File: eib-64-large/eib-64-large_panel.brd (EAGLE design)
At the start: 180 x 180 mm, 228 parts, among them J1 DF40-REC, J2 DF40-REC, J3 DF40-REC, J4 DF40-REC, J5 DF40-REC, J6 DF40-REC, J7 DF40-REC, J8 DF40-REC, J9 DF40-REC

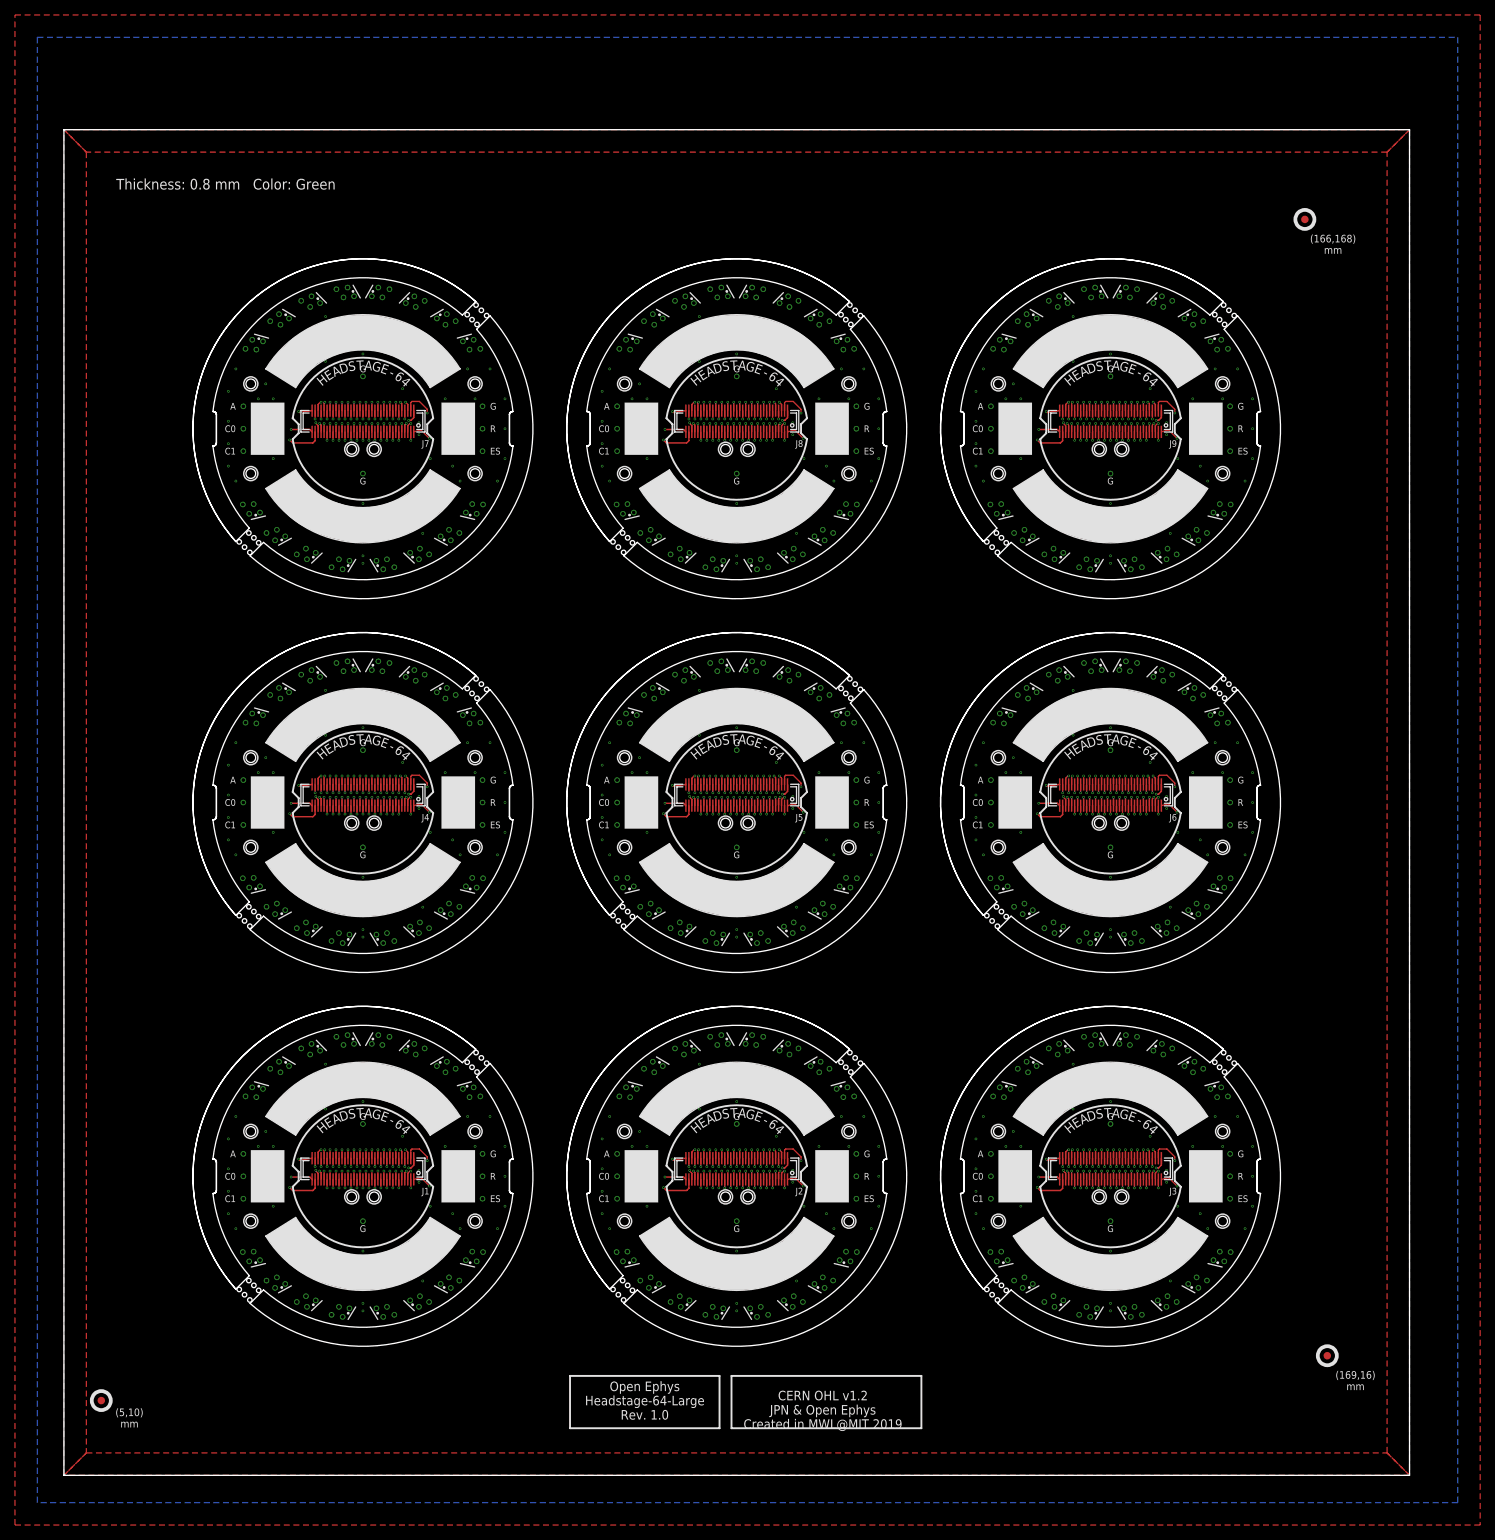
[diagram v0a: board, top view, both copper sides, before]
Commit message: headstage-64 rev. 1.4 along with all dependencies
- This is headstage-64 revision 1.4. Because it involves a change in the
bottom analog connector, a lot of other boards had to be changed to
match the new pinout. That is why there are so many files in this
commit. Changes in revision 1.4 and affects on other boards are as
follows:

1. The coaxial adapter board has been improved to allow a regulator to
sit on the daughter board. To do this, the filtered vcoax had to brought
back to the daughter board and then out again after regulation. Of
course this regulation can be bypassed simply by connecting these
contacts

2. Vcoax decoupling has been greatly improved to lower impedance of
power input. There is now 70 uF of decoupling capacitance on the
post-regulated vcoax.

3. The JTAG interface was changed to allow it to be enabled and disabled
by the programmer. This means that these pins are nominally used for
extra IO. The programmer now contains a jumper that allows it operate in
this new mode (closed) or legacy mode (open) for headstage-64 rev 1.3.

4. All of the serializers GPIO lines are now all routed to the FPGA.

5. The opto and estim circuits no longer share SPI lines so they can be
operated independently.

6. The analog routing to the intan chip has been changed such that the
electrode lines are shielded from vcoax, which was polluting the anlog
signals, by a ground pin. This means that eibs etc. need to respect this
new pinout. This is why eib-64, eib-64-large, nanoz-adapter,
omnetics-adapter-64, and test-board-64 have been changed.

7. The serializer on headstage-64 has been upgraded to DS90UB933-Q1
which has reduced back channel latencies, increased forward channel
bandwidth, and improved performance with
imperfect cabling.

8. There is a solder jumper on the bottom of headstage-64 to allow the
addition of an external resistor to AUXIN3 on the intan to allow it to
operate at lower bandwidths. This comes at the cost of not being able to
measure istim unless t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
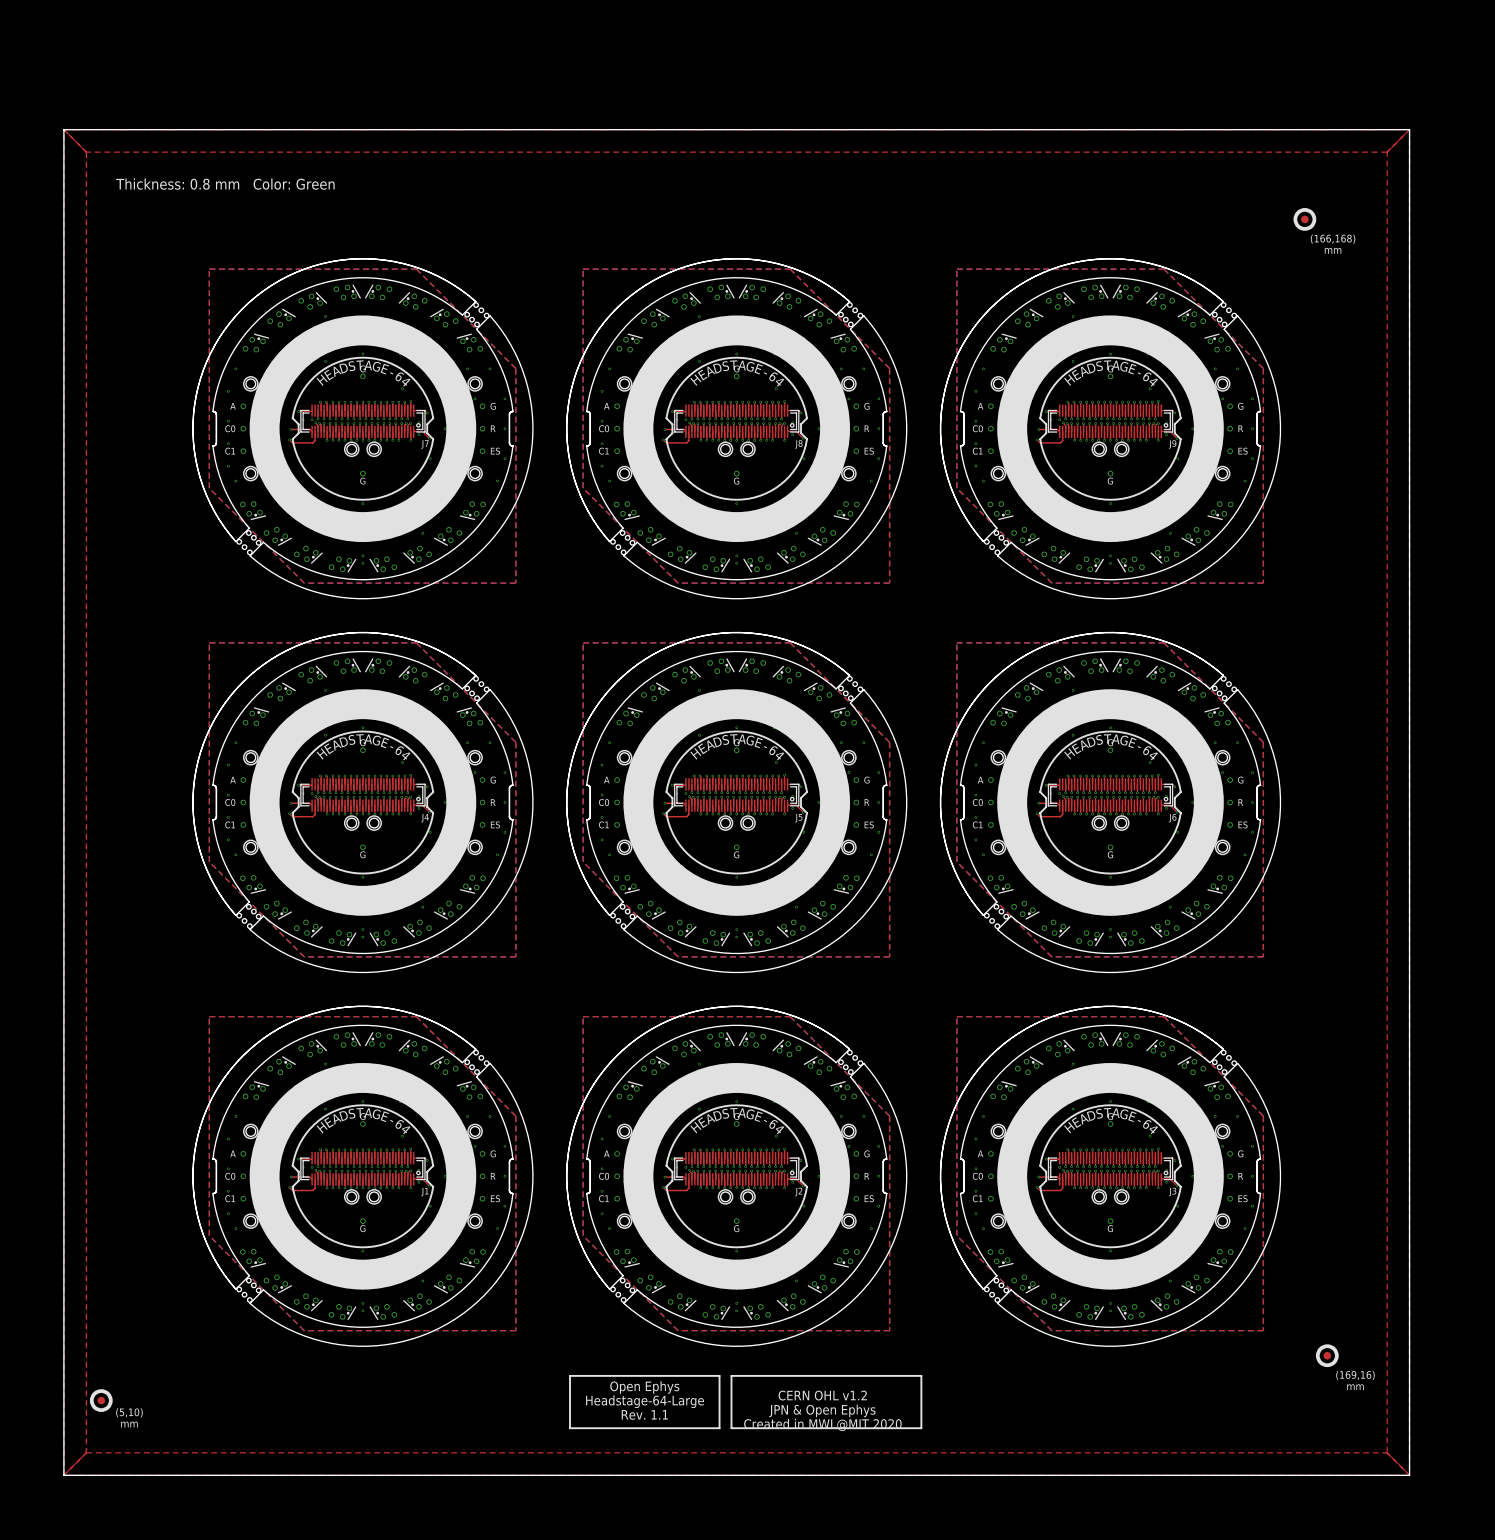
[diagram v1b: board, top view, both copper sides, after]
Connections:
- removed net GND: GND0.P$1, GND1.P$1, GND10.P$1, GND11.P$1, GND12.P$1, GND13.P$1, GND14.P$1, GND15.P$1, GND16.P$1, GND17.P$1, GND2.P$1, GND3.P$1, GND4.P$1, GND5.P$1, GND6.P$1, GND7.P$1, GND8.P$1, GND9.P$1, J1.70, J2.70, J3.70, J4.70, J5.70, J6.70, J7.70, J8.70, J9.70, SHLD_A.P$1, SHLD_A1.P$1, SHLD_A2.P$1, SHLD_A3.P$1, SHLD_A4.P$1, SHLD_A5.P$1, SHLD_A6.P$1, SHLD_A7.P$1, SHLD_A8.P$1
- new net GND1: GND0.P$1, GND1.P$1, J1.37, SHLD_A.P$1
- new net GND2: GND2.P$1, GND3.P$1, J2.37, SHLD_A1.P$1
- new net GND3: GND4.P$1, GND5.P$1, J3.37, SHLD_A2.P$1
- new net GND4: GND6.P$1, GND7.P$1, J4.37, SHLD_A3.P$1
- new net GND5: GND8.P$1, GND9.P$1, J5.37, SHLD_A4.P$1
- new net GND6: GND10.P$1, GND11.P$1, J6.37, SHLD_A5.P$1
- new net GND7: GND12.P$1, GND13.P$1, J7.37, SHLD_A6.P$1
- new net GND8: GND14.P$1, GND15.P$1, J8.37, SHLD_A7.P$1
- new net GND9: GND16.P$1, GND17.P$1, J9.37, SHLD_A8.P$1
- net N$1: now also J1.69; no longer J1.68
- net N$10: now also J1.60; no longer J1.59
- net N$100: now also J2.38; no longer J2.37
- net N$11: now also J1.59; no longer J1.58
- net N$12: now also J1.58; no longer J1.57
- net N$129: now also J3.69; no longer J3.68
- net N$13: now also J1.57; no longer J1.56
- net N$130: now also J3.67; no longer J3.66
- net N$131: now also J3.65; no longer J3.64
- net N$132: now also J3.64; no longer J3.63
- net N$133: now also J3.63; no longer J3.62
- net N$134: now also J3.62; no longer J3.61
- net N$135: now also J3.61; no longer J3.60
- net N$136: now also J3.60; no longer J3.59
- net N$137: now also J3.59; no longer J3.58
- net N$138: now also J3.58; no longer J3.57
- net N$139: now also J3.57; no longer J3.56
- net N$14: now also J1.56; no longer J1.55
- net N$140: now also J3.56; no longer J3.55
- net N$141: now also J3.55; no longer J3.54
- net N$142: now also J3.54; no longer J3.53
- net N$143: now also J3.53; no longer J3.52
- net N$144: now also J3.52; no longer J3.51
- net N$145: now also J3.51; no longer J3.50
- net N$146: now also J3.50; no longer J3.49
- net N$147: now also J3.49; no longer J3.48
- net N$148: now also J3.48; no longer J3.47
- net N$149: now also J3.47; no longer J3.46
- net N$15: now also J1.55; no longer J1.54
- net N$150: now also J3.46; no longer J3.45
- net N$151: now also J3.45; no longer J3.44
- net N$152: now also J3.44; no longer J3.43
- net N$153: now also J3.43; no longer J3.42
- net N$154: now also J3.42; no longer J3.41
- net N$155: now also J3.41; no longer J3.40
- net N$156: now also J3.39; no longer J3.38
- net N$16: now also J1.54; no longer J1.53
- net N$161: now also J3.66; no longer J3.65
- net N$162: now also J3.68; no longer J3.67
- net N$163: now also J3.40; no longer J3.39
- net N$164: now also J3.38; no longer J3.37
- net N$17: now also J1.53; no longer J1.52
- net N$18: now also J1.52; no longer J1.51
- net N$19: now also J1.51; no longer J1.50
- net N$193: now also J4.69; no longer J4.68
- net N$194: now also J4.67; no longer J4.66
- net N$195: now also J4.65; no longer J4.64
- net N$196: now also J4.64; no longer J4.63
- net N$197: now also J4.63; no longer J4.62
- net N$198: now also J4.62; no longer J4.61
- net N$2: now also J1.66; no longer J1.65
- net N$20: now also J1.50; no longer J1.49
- net N$21: now also J1.49; no longer J1.48
- net N$22: now also J1.48; no longer J1.47
- net N$227: now also J4.61; no longer J4.60
- net N$228: now also J4.60; no longer J4.59
- net N$229: now also J4.59; no longer J4.58
- net N$23: now also J1.47; no longer J1.46
- net N$230: now also J4.58; no longer J4.57
- net N$231: now also J4.57; no longer J4.56
- net N$232: now also J4.56; no longer J4.55
- net N$233: now also J4.55; no longer J4.54
- net N$234: now also J4.54; no longer J4.53
- net N$235: now also J4.53; no longer J4.52
- net N$236: now also J4.52; no longer J4.51
- net N$237: now also J4.51; no longer J4.50
- net N$238: now also J4.50; no longer J4.49
- net N$239: now also J4.49; no longer J4.48
- net N$24: now also J1.46; no longer J1.45
- net N$240: now also J4.48; no longer J4.47
- net N$241: now also J4.47; no longer J4.46
- net N$242: now also J4.46; no longer J4.45
- net N$243: now also J4.45; no longer J4.44
- net N$244: now also J4.44; no longer J4.43
- net N$245: now also J4.43; no longer J4.42
- net N$246: now also J4.42; no longer J4.41
- net N$247: now also J4.41; no longer J4.40
- net N$248: now also J4.39; no longer J4.38
- net N$25: now also J1.45; no longer J1.44
- net N$253: now also J4.66; no longer J4.65
- net N$254: now also J4.68; no longer J4.67
- net N$255: now also J4.40; no longer J4.39
- net N$256: now also J4.38; no longer J4.37
- net N$26: now also J1.44; no longer J1.43
- net N$27: now also J1.43; no longer J1.42
- net N$28: now also J1.42; no longer J1.41
- net N$285: now also J5.69; no longer J5.68
- net N$286: now also J5.67; no longer J5.66
- net N$287: now also J5.65; no longer J5.64
- net N$288: now also J5.64; no longer J5.63
- net N$289: now also J5.63; no longer J5.62
- net N$29: now also J1.41; no longer J1.40
- net N$290: now also J5.62; no longer J5.61
- net N$291: now also J5.61; no longer J5.60
- net N$292: now also J5.60; no longer J5.59
- net N$293: now also J5.59; no longer J5.58
- net N$294: now also J5.58; no longer J5.57
- net N$295: now also J5.57; no longer J5.56
- net N$296: now also J5.56; no longer J5.55
- net N$297: now also J5.55; no longer J5.54
- net N$298: now also J5.54; no longer J5.53
- net N$299: now also J5.53; no longer J5.52
- net N$3: now also J1.67; no longer J1.66
- net N$30: now also J1.40; no longer J1.39
- net N$300: now also J5.52; no longer J5.51
- net N$301: now also J5.51; no longer J5.50
- net N$302: now also J5.50; no longer J5.49
- net N$303: now also J5.49; no longer J5.48
- net N$304: now also J5.48; no longer J5.47
- net N$305: now also J5.47; no longer J5.46
- net N$306: now also J5.46; no longer J5.45
- net N$307: now also J5.45; no longer J5.44
- net N$308: now also J5.44; no longer J5.43
- net N$309: now also J5.43; no longer J5.42
- net N$31: now also J1.39; no longer J1.38
- net N$310: now also J5.42; no longer J5.41
- net N$311: now also J5.41; no longer J5.40
- net N$312: now also J5.39; no longer J5.38
- net N$317: now also J5.66; no longer J5.65
- net N$318: now also J5.68; no longer J5.67
- net N$319: now also J5.40; no longer J5.39
- net N$32: now also J1.38; no longer J1.37
- net N$320: now also J5.38; no longer J5.37
- net N$349: now also J6.69; no longer J6.68
- net N$350: now also J6.67; no longer J6.66
- net N$351: now also J6.65; no longer J6.64
- net N$352: now also J6.64; no longer J6.63
- net N$353: now also J6.63; no longer J6.62
- net N$354: now also J6.62; no longer J6.61
- net N$355: now also J6.61; no longer J6.60
- net N$356: now also J6.60; no longer J6.59
- net N$357: now also J6.59; no longer J6.58
- net N$358: now also J6.58; no longer J6.57
- net N$359: now also J6.57; no longer J6.56
- net N$360: now also J6.56; no longer J6.55
- net N$361: now also J6.55; no longer J6.54
- net N$362: now also J6.54; no longer J6.53
- net N$363: now also J6.53; no longer J6.52
- net N$364: now also J6.52; no longer J6.51
- net N$365: now also J6.51; no longer J6.50
- net N$366: now also J6.50; no longer J6.49
- net N$367: now also J6.49; no longer J6.48
- net N$368: now also J6.48; no longer J6.47
- net N$369: now also J6.47; no longer J6.46
- net N$370: now also J6.46; no longer J6.45
- net N$371: now also J6.45; no longer J6.44
- net N$372: now also J6.44; no longer J6.43
- net N$373: now also J6.43; no longer J6.42
- net N$374: now also J6.42; no longer J6.41
- net N$375: now also J6.41; no longer J6.40
- net N$376: now also J6.39; no longer J6.38
- net N$381: now also J6.66; no longer J6.65
- net N$382: now also J6.68; no longer J6.67
- net N$383: now also J6.40; no longer J6.39
- net N$384: now also J6.38; no longer J6.37
- net N$4: now also J1.68; no longer J1.67
- net N$413: now also J7.69; no longer J7.68
- net N$414: now also J7.67; no longer J7.66
- net N$415: now also J7.65; no longer J7.64
- net N$416: now also J7.64; no longer J7.63
- net N$417: now also J7.63; no longer J7.62
- net N$418: now also J7.62; no longer J7.61
- net N$419: now also J7.61; no longer J7.60
- net N$420: now also J7.60; no longer J7.59
- net N$421: now also J7.59; no longer J7.58
- net N$422: now also J7.58; no longer J7.57
- net N$423: now also J7.57; no longer J7.56
- net N$424: now also J7.56; no longer J7.55
- net N$425: now also J7.55; no longer J7.54
- net N$426: now also J7.54; no longer J7.53
- net N$427: now also J7.53; no longer J7.52
- net N$428: now also J7.52; no longer J7.51
- net N$429: now also J7.51; no longer J7.50
- net N$430: now also J7.50; no longer J7.49
- net N$431: now also J7.49; no longer J7.48
- net N$432: now also J7.48; no longer J7.47
- net N$433: now also J7.47; no longer J7.46
- net N$434: now also J7.46; no longer J7.45
- net N$435: now also J7.45; no longer J7.44
- net N$436: now also J7.44; no longer J7.43
- net N$437: now also J7.43; no longer J7.42
- net N$438: now also J7.42; no longer J7.41
- net N$439: now also J7.41; no longer J7.40
- net N$440: now also J7.39; no longer J7.38
- net N$445: now also J7.66; no longer J7.65
- net N$446: now also J7.68; no longer J7.67
- net N$447: now also J7.40; no longer J7.39
- net N$448: now also J7.38; no longer J7.37
- net N$477: now also J8.69; no longer J8.68
- net N$478: now also J8.67; no longer J8.66
- net N$479: now also J8.65; no longer J8.64
- net N$480: now also J8.64; no longer J8.63
- net N$481: now also J8.63; no longer J8.62
- net N$482: now also J8.62; no longer J8.61
- net N$483: now also J8.61; no longer J8.60
- net N$484: now also J8.60; no longer J8.59
- net N$485: now also J8.59; no longer J8.58
- net N$486: now also J8.58; no longer J8.57
- net N$487: now also J8.57; no longer J8.56
- net N$488: now also J8.56; no longer J8.55
- net N$489: now also J8.55; no longer J8.54
- net N$490: now also J8.54; no longer J8.53
- net N$491: now also J8.53; no longer J8.52
- net N$492: now also J8.52; no longer J8.51
- net N$493: now also J8.51; no longer J8.50
- net N$494: now also J8.50; no longer J8.49
- net N$495: now also J8.49; no longer J8.48
- net N$496: now also J8.48; no longer J8.47
- net N$497: now also J8.47; no longer J8.46
- net N$498: now also J8.46; no longer J8.45
- net N$499: now also J8.45; no longer J8.44
- net N$5: now also J1.65; no longer J1.64
- net N$500: now also J8.44; no longer J8.43
- net N$501: now also J8.43; no longer J8.42
- net N$502: now also J8.42; no longer J8.41
- net N$503: now also J8.41; no longer J8.40
- net N$504: now also J8.39; no longer J8.38
- net N$509: now also J8.66; no longer J8.65
- net N$510: now also J8.68; no longer J8.67
- net N$511: now also J8.40; no longer J8.39
- net N$512: now also J8.38; no longer J8.37
- net N$541: now also J9.69; no longer J9.68
- net N$542: now also J9.67; no longer J9.66
- net N$543: now also J9.65; no longer J9.64
- net N$544: now also J9.64; no longer J9.63
- net N$545: now also J9.63; no longer J9.62
- net N$546: now also J9.62; no longer J9.61
- net N$547: now also J9.61; no longer J9.60
- net N$548: now also J9.60; no longer J9.59
- net N$549: now also J9.59; no longer J9.58
- net N$550: now also J9.58; no longer J9.57
- net N$551: now also J9.57; no longer J9.56
- net N$552: now also J9.56; no longer J9.55
- net N$553: now also J9.55; no longer J9.54
- net N$554: now also J9.54; no longer J9.53
- net N$555: now also J9.53; no longer J9.52
- net N$556: now also J9.52; no longer J9.51
- net N$557: now also J9.51; no longer J9.50
- net N$558: now also J9.50; no longer J9.49
- net N$559: now also J9.49; no longer J9.48
- net N$560: now also J9.48; no longer J9.47
- net N$561: now also J9.47; no longer J9.46
- net N$562: now also J9.46; no longer J9.45
- net N$563: now also J9.45; no longer J9.44
- net N$564: now also J9.44; no longer J9.43
- net N$565: now also J9.43; no longer J9.42
- net N$566: now also J9.42; no longer J9.41
- net N$567: now also J9.41; no longer J9.40
- net N$568: now also J9.39; no longer J9.38
- net N$573: now also J9.66; no longer J9.65
- net N$574: now also J9.68; no longer J9.67
- net N$575: now also J9.40; no longer J9.39
- net N$576: now also J9.38; no longer J9.37
- net N$6: now also J1.64; no longer J1.63
- net N$65: now also J2.69; no longer J2.68
- net N$66: now also J2.67; no longer J2.66
- net N$67: now also J2.65; no longer J2.64
- net N$68: now also J2.64; no longer J2.63
- net N$69: now also J2.63; no longer J2.62
- net N$7: now also J1.63; no longer J1.62
- net N$70: now also J2.62; no longer J2.61
- net N$71: now also J2.61; no longer J2.60
- net N$72: now also J2.60; no longer J2.59
- net N$73: now also J2.59; no longer J2.58
- net N$74: now also J2.58; no longer J2.57
- net N$75: now also J2.57; no longer J2.56
- net N$76: now also J2.56; no longer J2.55
- net N$77: now also J2.55; no longer J2.54
- net N$78: now also J2.54; no longer J2.53
- net N$79: now also J2.53; no longer J2.52
- net N$8: now also J1.62; no longer J1.61
- net N$80: now also J2.52; no longer J2.51
- net N$81: now also J2.51; no longer J2.50
- net N$82: now also J2.50; no longer J2.49
- net N$83: now also J2.49; no longer J2.48
- net N$84: now also J2.48; no longer J2.47
- net N$85: now also J2.47; no longer J2.46
- net N$86: now also J2.46; no longer J2.45
- net N$87: now also J2.45; no longer J2.44
- net N$88: now also J2.44; no longer J2.43
- net N$89: now also J2.43; no longer J2.42
- net N$9: now also J1.61; no longer J1.60
- net N$90: now also J2.42; no longer J2.41
- net N$91: now also J2.41; no longer J2.40
- net N$92: now also J2.39; no longer J2.38
- net N$97: now also J2.66; no longer J2.65
- net N$98: now also J2.68; no longer J2.67
- net N$99: now also J2.40; no longer J2.39
- net REF: now also J1.70; no longer J1.69
- net REF1: now also J2.70; no longer J2.69
- net REF2: now also J3.70; no longer J3.69
- net REF3: now also J4.70; no longer J4.69
- net REF4: now also J5.70; no longer J5.69
- net REF5: now also J6.70; no longer J6.69
- net REF6: now also J7.70; no longer J7.69
- net REF7: now also J8.70; no longer J8.69
- net REF8: now also J9.70; no longer J9.69
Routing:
- net GND: track 16.0 -> 0.00 mm, vias 423 -> 0
- net REF8: track 12.5 -> 10.2 mm
- net REF6: track 12.5 -> 10.2 mm
- net REF7: track 12.5 -> 10.2 mm
- net REF5: track 12.5 -> 10.2 mm
- net REF3: track 12.5 -> 10.2 mm
- net REF2: track 12.5 -> 10.2 mm
- net REF4: track 12.5 -> 10.2 mm
- net REF: track 12.5 -> 10.2 mm
- net REF1: track 12.5 -> 10.2 mm
- net N$129: track 14.2 -> 13.4 mm
- net N$541: track 14.2 -> 13.4 mm
- net N$349: track 14.2 -> 13.4 mm
- net N$65: track 14.2 -> 13.4 mm
- net N$477: track 14.2 -> 13.4 mm
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- added copper zone on layer 1, net GND1
- added copper zone on layer 15, net GND1
- added copper zone on layer 16, net GND1
- added copper zone on layer 2, net GND1
- added copper zone on layer 1, net GND2
- added copper zone on layer 15, net GND2
- added copper zone on layer 16, net GND2
- added copper zone on layer 2, net GND2
- added copper zone on layer 1, net GND3
- added copper zone on layer 15, net GND3
- added copper zone on layer 16, net GND3
- added copper zone on layer 2, net GND3
- added copper zone on layer 1, net GND4
- added copper zone on layer 15, net GND4
- added copper zone on layer 16, net GND4
- added copper zone on layer 2, net GND4
- added copper zone on layer 1, net GND5
- added copper zone on layer 15, net GND5
- added copper zone on layer 16, net GND5
- added copper zone on layer 2, net GND5
- added copper zone on layer 1, net GND6
- added copper zone on layer 15, net GND6
- added copper zone on layer 16, net GND6
- added copper zone on layer 2, net GND6
- added copper zone on layer 1, net GND7
- added copper zone on layer 15, net GND7
- added copper zone on layer 16, net GND7
- added copper zone on layer 2, net GND7
- added copper zone on layer 1, net GND8
- added copper zone on layer 15, net GND8
- added copper zone on layer 16, net GND8
- added copper zone on layer 2, net GND8
- added copper zone on layer 1, net GND9
- added copper zone on layer 15, net GND9
- added copper zone on layer 16, net GND9
- added copper zone on layer 2, net GND9
- removed copper zone on layer 1, net GND
- removed copper zone on layer 15, net GND
- removed copper zone on layer 16, net GND
- removed copper zone on layer 2, net GND
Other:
- board text added: "CERN OHL v1.2 JPN & Open Ephys Created in MWL@MIT 2020"
- board text added: "Open Ephys Headstage-64-Large Rev. 1.1"
- board text added: "Rev. 1.1 CERN OHL v1.2 JPN & Open Ephys 2019"
- board text removed: "CERN OHL v1.2 JPN & Open Ephys Created in MWL@MIT 2019"
- board text removed: "Open Ephys Headstage-64-Large Rev. 1.0"
- board text removed: "Rev. 1.0 CERN OHL v1.2 JPN & Open Ephys 2019"
